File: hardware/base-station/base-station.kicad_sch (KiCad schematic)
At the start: 6 parts

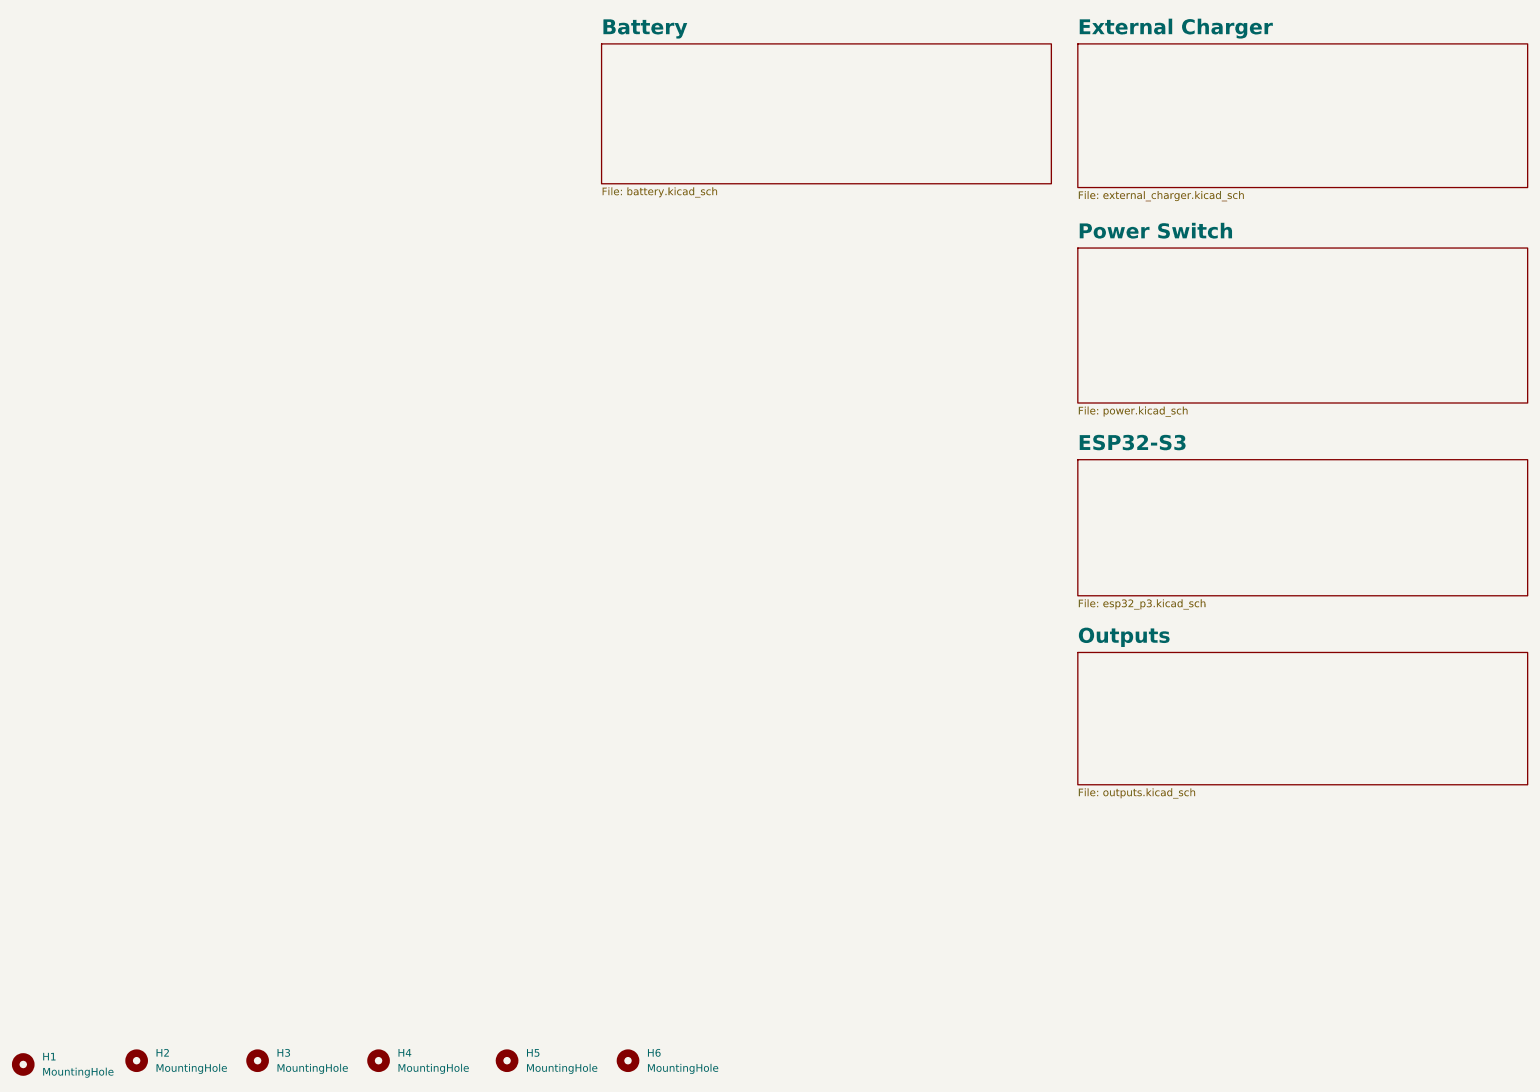
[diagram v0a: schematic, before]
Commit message: hardware: battery protection, boost swap, and a capacitor voltage audit
Base station power chain, all verified against exported netlists:

- Protection: MAX17303G+ gauge/protector and its NTMD6N02R2G FET pair
  replaced by DW01A + 2x FS8205A. The MAX17303 had no firmware driver and
  the board never had a working coulomb counter, so state of charge already
  came from the voltage curve in bs_battery_soc.h; it now reads a 1M/1M
  divider on GPIO1. The FETs move from the positive rail to the negative
  one because the DW01A has no charge pump, so board ground is now P-,
  separated from the cell's B- by the FET stack. Two FS8205A in parallel
  put the 150 mV overcurrent trip at ~4.8-6.0 A instead of ~2.4-3.0 A.
  TH1 moves onto the BQ21040's TS pin, replacing a fixed 10k that had been
  defeating thermal charge cutoff.

- V_LORA retargeted 7.49 V -> 4.95 V and LM5157QRTERQ1 -> TPS61023DRLR.
  Nothing needed 7.4 V (everything downstream is 3.3 V behind the
  TPS62913), while an RFD868x-class radio is 5 V nominal with a 6 V
  absolute maximum, so the old rail put it permanently out of reach. Being
  synchronous and internally compensated also dropped D2, C35-C38 and R10.
  Inductor stays the fleet 2.2 uH: inside TI's 0.37-2.9 uH range and the
  only value meeting their ripple-under-40%-of-average guidance at load.

- Keystone 1043P holder -> MYOUNG BH-18650-A5BJ001-2D. Terminal pitch
  72.30 vs 72.22 mm, so the battery nets did not move; BT2 is rotated 180
  degrees because this part's positive end is mirrored.

Across all four boards:

- Every crystal was mis-loaded. 32.768 kHz parts saw ~9 pF against a 6 pF
  spec and the 40 MHz saw 12.5 pF against 10 pF, both pulling slow. Moved
  to Seiko SC-32S (12.5 pF) with 22 pF load caps, and the 40 MHz caps to
  18 pF. The tolerance being paid for had been swamped several times over.

- Capacitor voltage audit, new Min V rating column in the BOM. Three parts
  were operating outside their rating on 8.4 V rails: 47 uF and 100 u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
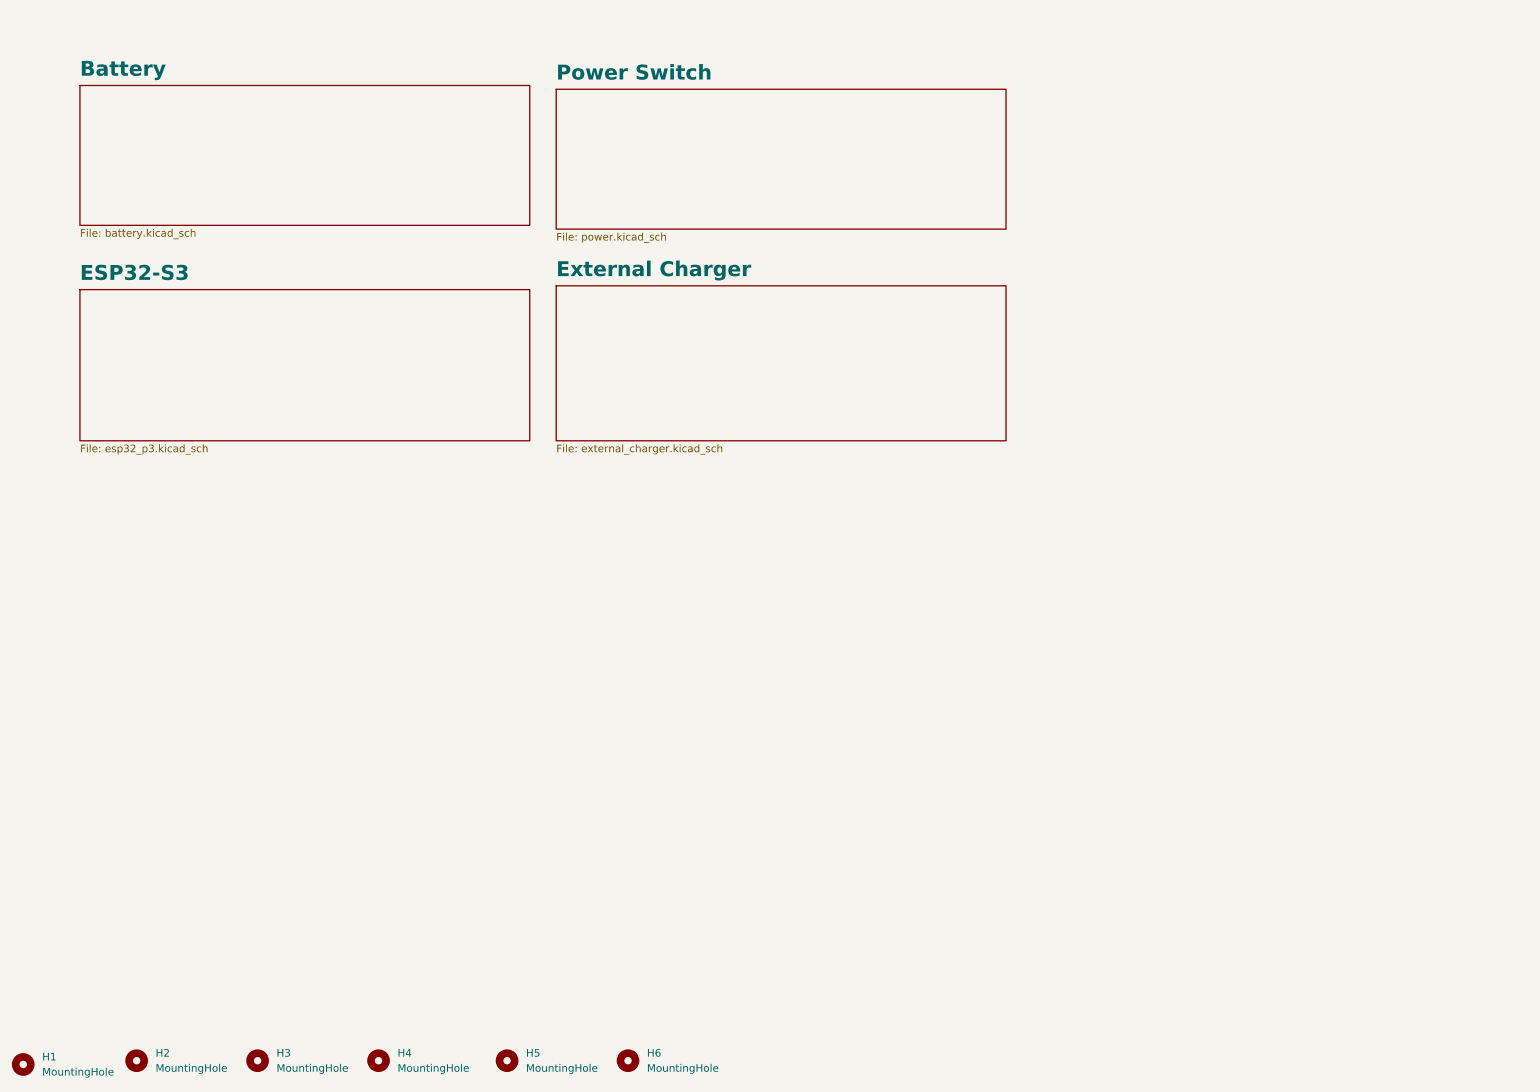
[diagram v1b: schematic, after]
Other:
- removed sheet Outputs
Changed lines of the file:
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@@
 	)
 	(sheet
-		(at 193.04 125.095)
-		(size 75.565 22.225)
-		(exclude_from_sim no)
-		(in_bom yes)
-		(on_board yes)
-		(dnp no)
-		(fields_autoplaced yes)
-		(stroke
-			(width 0.1524)
-			(type solid)
-		)
-		(fill
-			(color 0 0 0 0)
-		)
-		(property "Sheetname" "Outputs"
-			(at 193.04 123.7684 0)
-			(show_name no)
-			(do_not_autoplace no)
-			(effects
-				(font
-					(size 2.5 2.5)
-					(thickness 0.5)
-					(bold yes)
-				)
-				(justify left bottom)
-			)
-		)
-		(property "Sheetfile" "outputs.kicad_sch"
-			(at 193.04 147.9046 0)
-			(show_name no)
-			(do_not_autoplace no)
-			(effects
-				(font
-					(size 1.27 1.27)
-				)
-				(justify left top)
-			)
-		)
-		(instances
-			(project "base-station"
-				(path "/d2421514-d142-4c71-ac69-48d30c1a771f"
-					(page "7")
-				)
-			)
-		)
-	)
-	(sheet
-		(at 113.03 22.86)
+		(at 25.4 29.845)
 		(size 75.565 23.495)
 		(exclude_from_sim no)
@@
 		)
 		(property "Sheetname" "Battery"
-			(at 113.03 21.5334 0)
+			(at 25.4 28.5184 0)
 			(show_name no)
 			(do_not_autoplace no)
@@
 		)
 		(property "Sheetfile" "battery.kicad_sch"
-			(at 113.03 46.9396 0)
+			(at 25.4 53.9246 0)
 			(show_name no)
 			(do_not_autoplace no)
@@
 	)
 	(sheet
-		(at 193.04 92.71)
-		(size 75.565 22.86)
+		(at 25.4 64.135)
+		(size 75.565 25.4)
 		(exclude_from_sim no)
 		(in_bom yes)
@@
 		)
 		(property "Sheetname" "ESP32-S3"
-			(at 193.04 91.3834 0)
+			(at 25.4 62.8084 0)
 			(show_name no)
 			(do_not_autoplace no)
@@
 		)
 		(property "Sheetfile" "esp32_p3.kicad_sch"
-			(at 193.04 116.1546 0)
+			(at 25.4 90.1196 0)
 			(show_name no)
 			(do_not_autoplace no)
@@
 	)
 	(sheet
-		(at 193.04 57.15)
-		(size 75.565 26.035)
+		(at 105.41 30.48)
+		(size 75.565 23.495)
 		(exclude_from_sim no)
 		(in_bom yes)
@@
 		)
 		(property "Sheetname" "Power Switch"
-			(at 193.04 55.8234 0)
+			(at 105.41 29.1534 0)
 			(show_name no)
 			(do_not_autoplace no)
@@
 		)
 		(property "Sheetfile" "power.kicad_sch"
-			(at 193.04 83.7696 0)
+			(at 105.41 54.5596 0)
 			(show_name no)
 			(do_not_autoplace no)
@@
 	)
 	(sheet
-		(at 193.04 22.86)
-		(size 75.565 24.13)
+		(at 105.41 63.5)
+		(size 75.565 26.035)
 		(exclude_from_sim no)
 		(in_bom yes)
@@
 		)
 		(property "Sheetname" "External Charger"
-			(at 193.04 21.5334 0)
+			(at 105.41 62.1734 0)
 			(show_name no)
 			(do_not_autoplace no)
@@
 		)
 		(property "Sheetfile" "external_charger.kicad_sch"
-			(at 193.04 47.5746 0)
+			(at 105.41 90.1196 0)
 			(show_name no)
 			(do_not_autoplace no)
